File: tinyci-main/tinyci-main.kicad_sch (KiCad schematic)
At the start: 47 parts

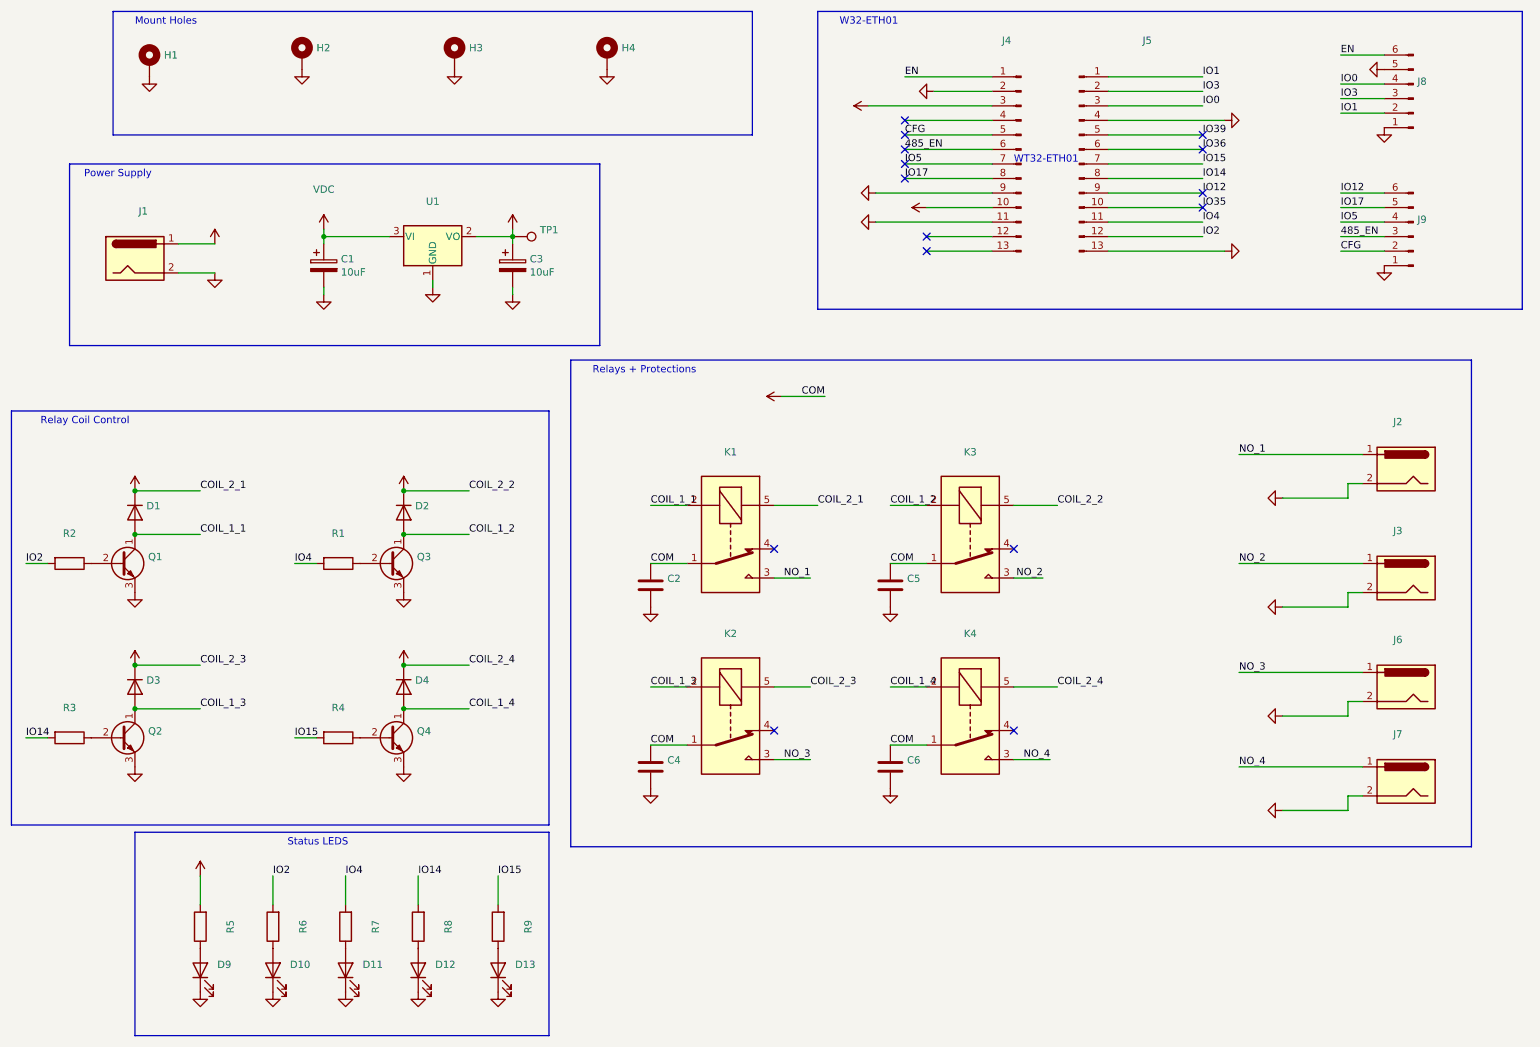
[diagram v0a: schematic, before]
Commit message: tinyci-main: Added stacked USB-A connectors to schematic so they are easier to route.
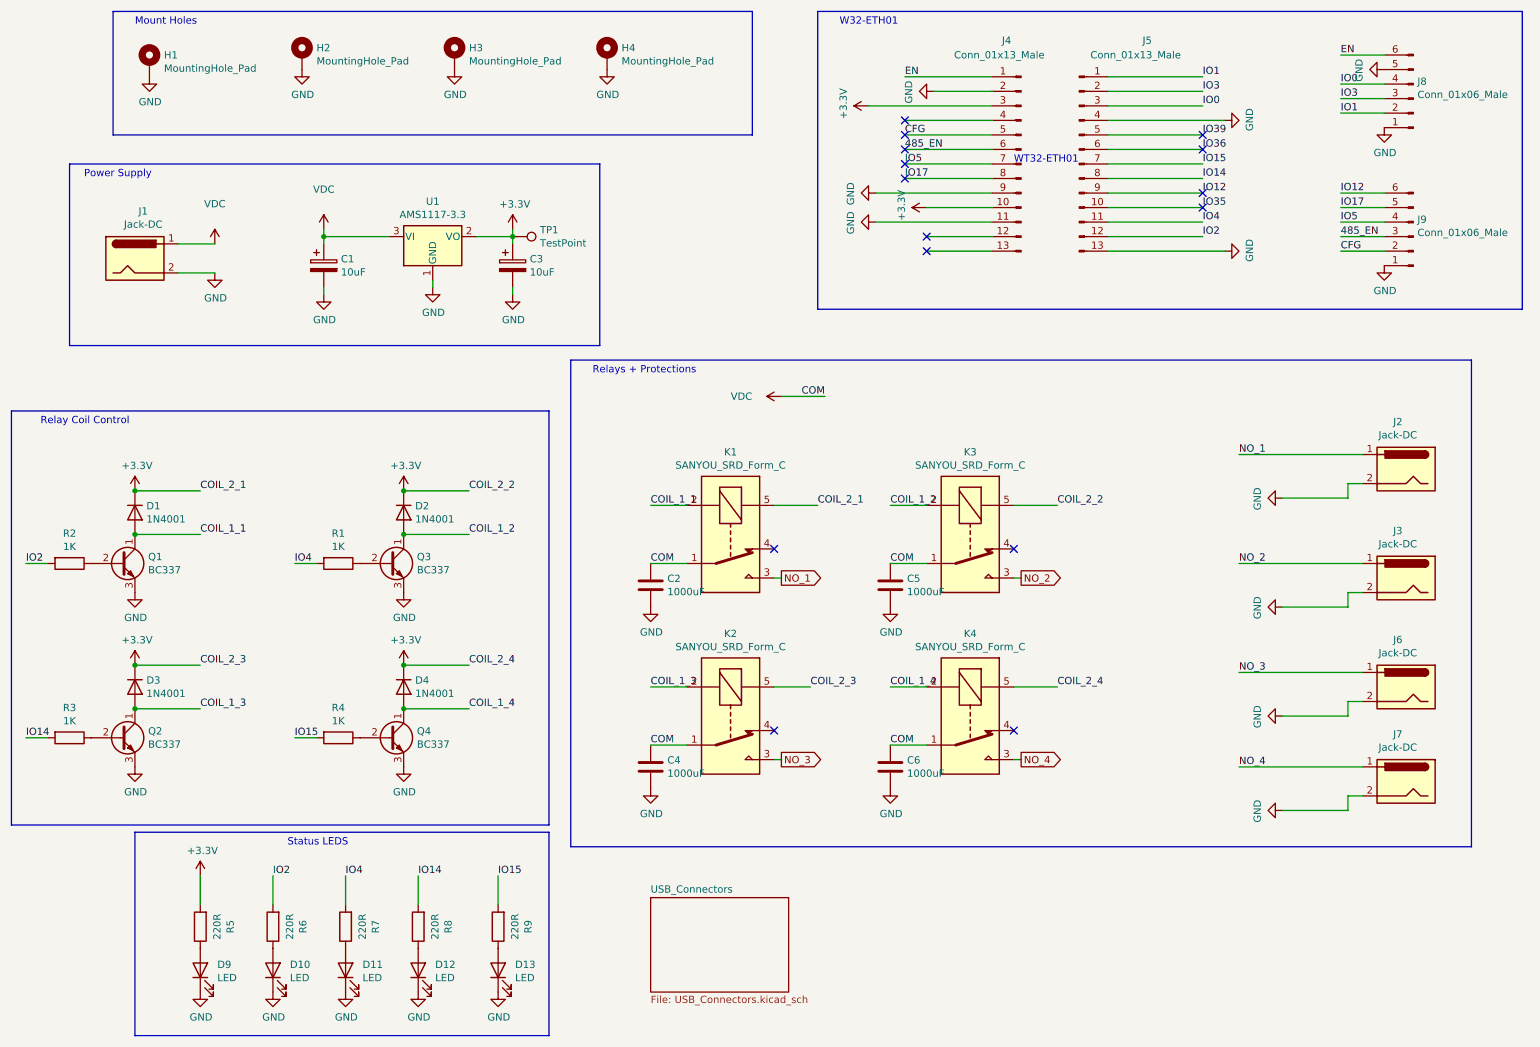
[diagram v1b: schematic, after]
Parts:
- C2, C4, C5, C6: value (none) -> 1000uF; footprint (none) -> Capacitor_THT:CP_Radial_D10.0mm_P5.00mm
- D1, D2, D3, D4: value (none) -> 1N4001; footprint (none) -> Diode_THT:D_DO-41_SOD81_P10.16mm_Horizontal
- D10, D11, D12, D13, D9: value (none) -> LED; footprint (none) -> LED_SMD:LED_1206_3216Metric
- H1, H2, H3, H4: value (none) -> MountingHole_Pad; footprint (none) -> MountingHole:MountingHole_3.2mm_M3_Pad
- J1, J2, J3, J6, J7: value (none) -> Jack-DC; footprint (none) -> Connector_BarrelJack:BarrelJack_Horizontal
- J4, J5: value (none) -> Conn_01x13_Male; footprint (none) -> Connector_PinHeader_2.54mm:PinHeader_1x13_P2.54mm_Vertical
- J8, J9: value (none) -> Conn_01x06_Male; footprint (none) -> Connector_PinHeader_2.54mm:PinHeader_1x06_P2.54mm_Vertical
- K1, K2, K3, K4: value (none) -> SANYOU_SRD_Form_C; footprint (none) -> Relay_THT:Relay_SPDT_SANYOU_SRD_Series_Form_C
- Q1, Q2, Q3, Q4: value (none) -> BC337; footprint (none) -> Package_TO_SOT_THT:TO-92_Inline
- R1, R2, R3, R4: value (none) -> 1K; footprint (none) -> Resistor_SMD:R_1206_3216Metric
- R5, R6, R7, R8, R9: value (none) -> 220R; footprint (none) -> Resistor_SMD:R_1206_3216Metric
- TP1: value (none) -> TestPoint; footprint (none) -> TestPoint:TestPoint_Pad_D2.0mm
- U1: value (none) -> AMS1117-3.3; footprint (none) -> Package_TO_SOT_SMD:SOT-223-3_TabPin2
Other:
- added sheet USB_Connectors (USB_Connectors.kicad_sch)

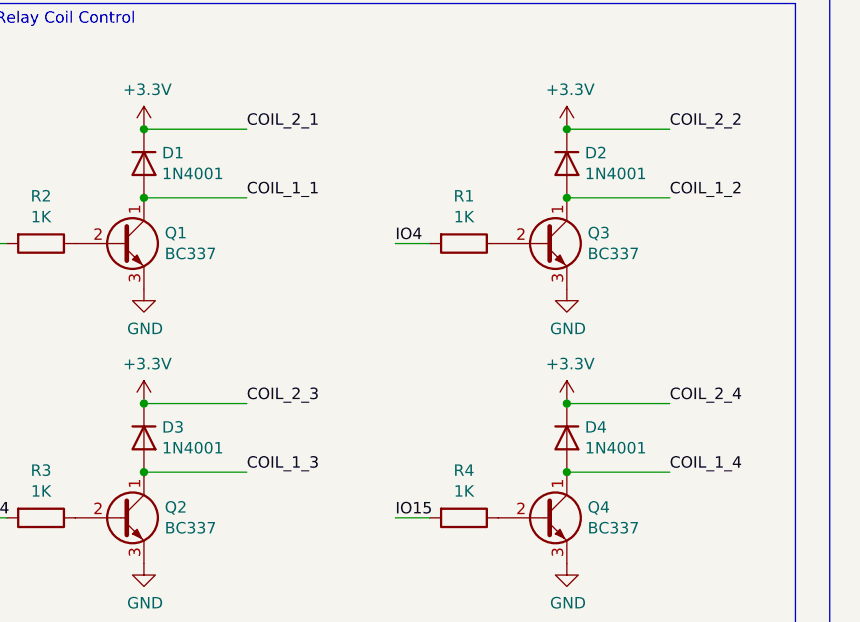
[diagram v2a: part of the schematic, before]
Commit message: tinyci-main: Replaced the relay coil flyback diodes by SMD parts to speed up the board assembly.
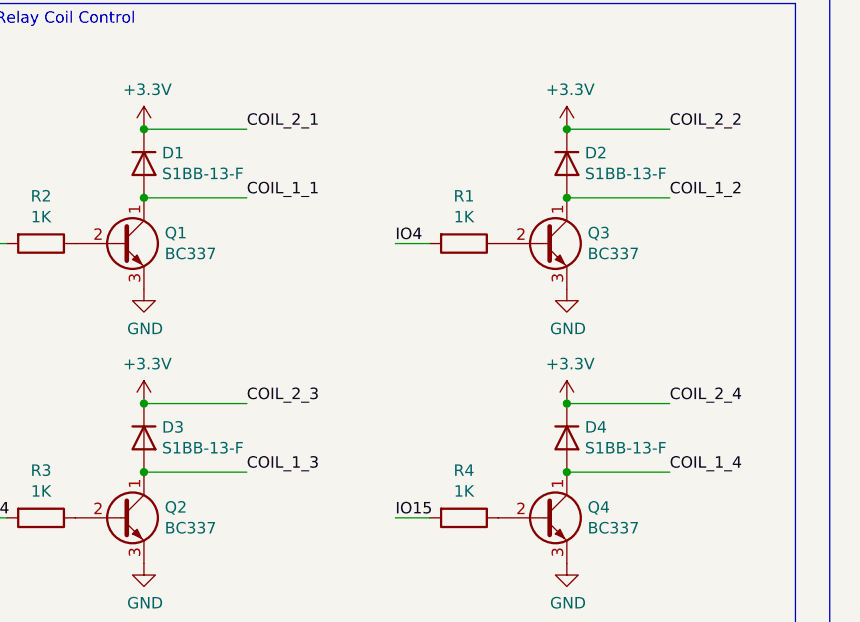
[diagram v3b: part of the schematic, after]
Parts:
- D1, D2, D3, D4: value 1N4001 -> S1BB-13-F; footprint Diode_THT:D_DO-41_SOD81_P10.16mm_Horizontal -> Diode_SMD:D_SMB_Handsoldering
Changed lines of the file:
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@@
       (effects (font (size 1.27 1.27)) (justify left))
     )
-    (property "Value" "1N4001" (id 1) (at 85.8266 106.553 90)
-      (effects (font (size 1.27 1.27)) (justify left))
-    )
-    (property "Footprint" "Diode_THT:D_DO-41_SOD81_P10.16mm_Horizontal" (id 2) (at 79.375 105.41 0)
-      (effects (font (size 1.27 1.27)) hide)
-    )
-    (property "Datasheet" "http://www.vishay.com/docs/88503/1n4001.pdf" (id 3) (at 83.82 105.41 0)
+    (property "Value" "S1BB-13-F" (id 1) (at 85.8266 106.553 90)
+      (effects (font (size 1.27 1.27)) (justify left))
+    )
+    (property "Footprint" "Diode_SMD:D_SMB_Handsoldering" (id 2) (at 79.375 105.41 0)
+      (effects (font (size 1.27 1.27)) hide)
+    )
+    (property "Datasheet" "~" (id 3) (at 83.82 105.41 0)
       (effects (font (size 1.27 1.27)) hide)
     )
@@
       (effects (font (size 1.27 1.27)) (justify left))
     )
-    (property "Value" "1N4001" (id 1) (at 38.8366 106.553 90)
-      (effects (font (size 1.27 1.27)) (justify left))
-    )
-    (property "Footprint" "Diode_THT:D_DO-41_SOD81_P10.16mm_Horizontal" (id 2) (at 32.385 105.41 0)
-      (effects (font (size 1.27 1.27)) hide)
-    )
-    (property "Datasheet" "http://www.vishay.com/docs/88503/1n4001.pdf" (id 3) (at 36.83 105.41 0)
+    (property "Value" "S1BB-13-F" (id 1) (at 38.8366 106.553 90)
+      (effects (font (size 1.27 1.27)) (justify left))
+    )
+    (property "Footprint" "Diode_SMD:D_SMB_Handsoldering" (id 2) (at 32.385 105.41 0)
+      (effects (font (size 1.27 1.27)) hide)
+    )
+    (property "Datasheet" "~" (id 3) (at 36.83 105.41 0)
       (effects (font (size 1.27 1.27)) hide)
     )
@@
       (effects (font (size 1.27 1.27)) (justify left))
     )
-    (property "Value" "1N4001" (id 1) (at 38.8366 137.033 90)
-      (effects (font (size 1.27 1.27)) (justify left))
-    )
-    (property "Footprint" "Diode_THT:D_DO-41_SOD81_P10.16mm_Horizontal" (id 2) (at 32.385 135.89 0)
-      (effects (font (size 1.27 1.27)) hide)
-    )
-    (property "Datasheet" "http://www.vishay.com/docs/88503/1n4001.pdf" (id 3) (at 36.83 135.89 0)
+    (property "Value" "S1BB-13-F" (id 1) (at 38.8366 137.033 90)
+      (effects (font (size 1.27 1.27)) (justify left))
+    )
+    (property "Footprint" "Diode_SMD:D_SMB_Handsoldering" (id 2) (at 32.385 135.89 0)
+      (effects (font (size 1.27 1.27)) hide)
+    )
+    (property "Datasheet" "~" (id 3) (at 36.83 135.89 0)
       (effects (font (size 1.27 1.27)) hide)
     )
@@
       (effects (font (size 1.27 1.27)) (justify left))
     )
-    (property "Value" "1N4001" (id 1) (at 85.8266 137.033 90)
-      (effects (font (size 1.27 1.27)) (justify left))
-    )
-    (property "Footprint" "Diode_THT:D_DO-41_SOD81_P10.16mm_Horizontal" (id 2) (at 79.375 135.89 0)
-      (effects (font (size 1.27 1.27)) hide)
-    )
-    (property "Datasheet" "http://www.vishay.com/docs/88503/1n4001.pdf" (id 3) (at 83.82 135.89 0)
+    (property "Value" "S1BB-13-F" (id 1) (at 85.8266 137.033 90)
+      (effects (font (size 1.27 1.27)) (justify left))
+    )
+    (property "Footprint" "Diode_SMD:D_SMB_Handsoldering" (id 2) (at 79.375 135.89 0)
+      (effects (font (size 1.27 1.27)) hide)
+    )
+    (property "Datasheet" "~" (id 3) (at 83.82 135.89 0)
       (effects (font (size 1.27 1.27)) hide)
     )
@@
     )
     (path "/00000000-0000-0000-0000-00005fae3422"
-      (reference "D1") (unit 1) (value "1N4001") (footprint "Diode_THT:D_DO-41_SOD81_P10.16mm_Horizontal")
+      (reference "D1") (unit 1) (value "S1BB-13-F") (footprint "Diode_SMD:D_SMB_Handsoldering")
     )
     (path "/00000000-0000-0000-0000-00005fa9f96e"
-      (reference "D2") (unit 1) (value "1N4001") (footprint "Diode_THT:D_DO-41_SOD81_P10.16mm_Horizontal")
+      (reference "D2") (unit 1) (value "S1BB-13-F") (footprint "Diode_SMD:D_SMB_Handsoldering")
     )
     (path "/00000000-0000-0000-0000-00005fae6202"
-      (reference "D3") (unit 1) (value "1N4001") (footprint "Diode_THT:D_DO-41_SOD81_P10.16mm_Horizontal")
+      (reference "D3") (unit 1) (value "S1BB-13-F") (footprint "Diode_SMD:D_SMB_Handsoldering")
     )
     (path "/00000000-0000-0000-0000-00005fae925a"
-      (reference "D4") (unit 1) (value "1N4001") (footprint "Diode_THT:D_DO-41_SOD81_P10.16mm_Horizontal")
+      (reference "D4") (unit 1) (value "S1BB-13-F") (footprint "Diode_SMD:D_SMB_Handsoldering")
     )
     (path "/00000000-0000-0000-0000-00005fb38527"
